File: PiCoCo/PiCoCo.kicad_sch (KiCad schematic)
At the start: 54 parts, among them P1 COCO-CART, Q2 2N7002, Q3 2N7002, Q4 2N7002, U1 Pico 2 / RP2350B-Plus-W, U10 SN74LVC245A, U11 SN74LVC245A, U12 SN74LVC245A, U13 SN74LVC245A, U14 AMS1117-3.3, U15 SN74LVC00A

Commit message: bom: U15 SN74LVC00ADR = LCSC C485072 (schematic, PCB fields, BOM.md, fab package)
Co-Authored-By: Claude Fable 5.1 <noreply@anthropic.com>
Claude-Session: https://claude.ai/code/session_013jbrP69zFzwzxjawTKy2c7
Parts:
- U15: LCSC (none) -> C485072; MPN SN74LVC00AD -> SN74LVC00ADR

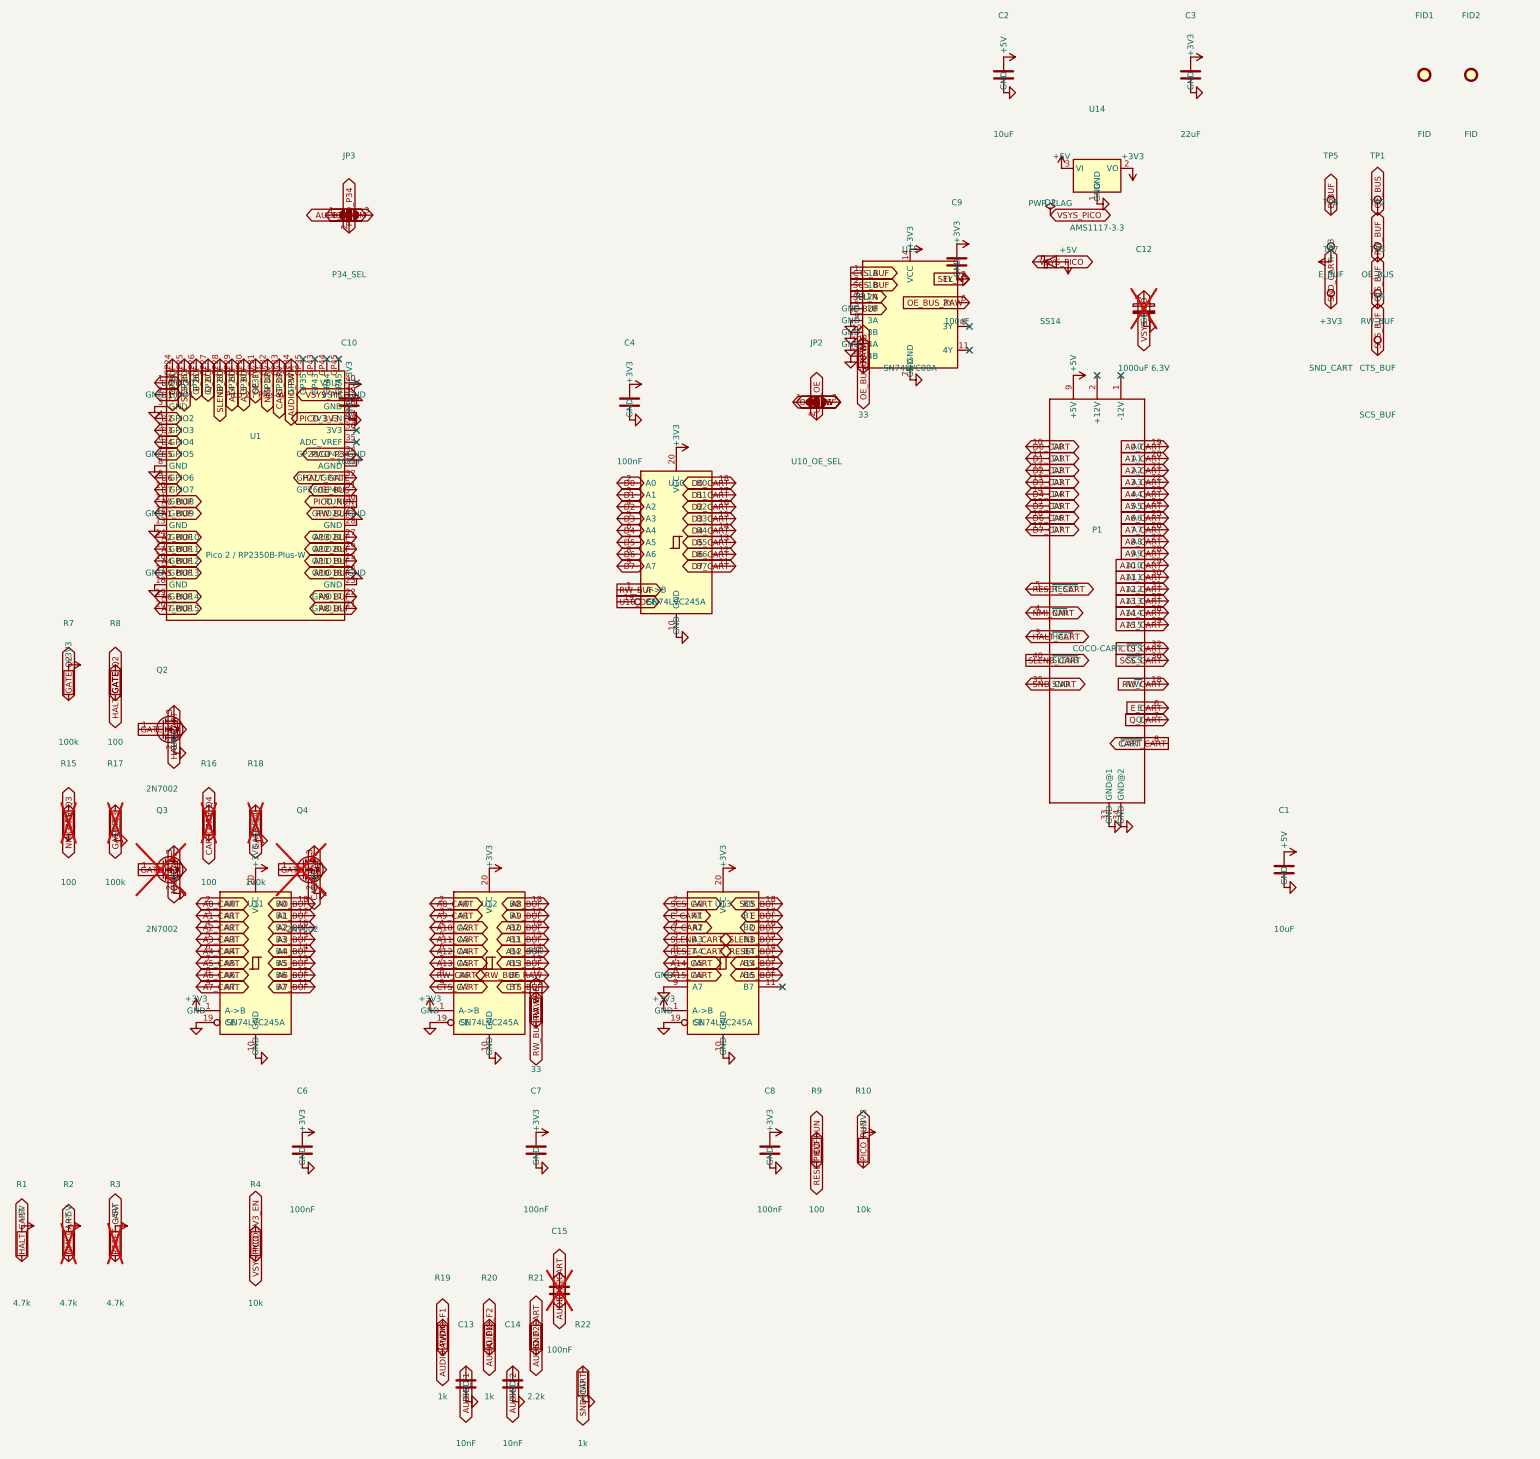
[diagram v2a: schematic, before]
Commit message: v2.3.1: body grown 12 mm, JP3 audio default, pre-order fixes (schematic, outline, docs)
Measured CoCo 3 opening 114.3 x 30.2 mm, connector face 43 mm inside the
case: the 98 mm body fits, but the module USB-C sat on the case surface.
Body is now 98 x 67.16 mm (+10.16 mm tongue); module, TPs, JP3, HDMI
reserve move up 12 mm.

Schematic (gen_schematic.py): R7 10k (RP2350 reset pull-down beat 100k),
R10 DNP (held RUN low when USB-only), R3 populated, R23 10k pull-up on
SLENB_CART (pin 40 is cart->CoCo), R25 10k pull-up on U10_OE, C15 1uF DNP
in series with R24 0R bypass (true AC-coupling option), JP4 Q->/CART
solder jumper (autostart tie), TP8 GND, FID3, JP3 pin 1 = AUDIO_PWM
(audio default), 100k LCSC C149504 (C17407 discontinued). Rev 2.3.1.

Docs, BOM, ordering checklist, breakout README (the tab-width note was
wrong) and spec §11 updated.

Co-Authored-By: Claude Fable 5.1 <noreply@anthropic.com>
Claude-Session: https://claude.ai/code/session_013jbrP69zFzwzxjawTKy2c7
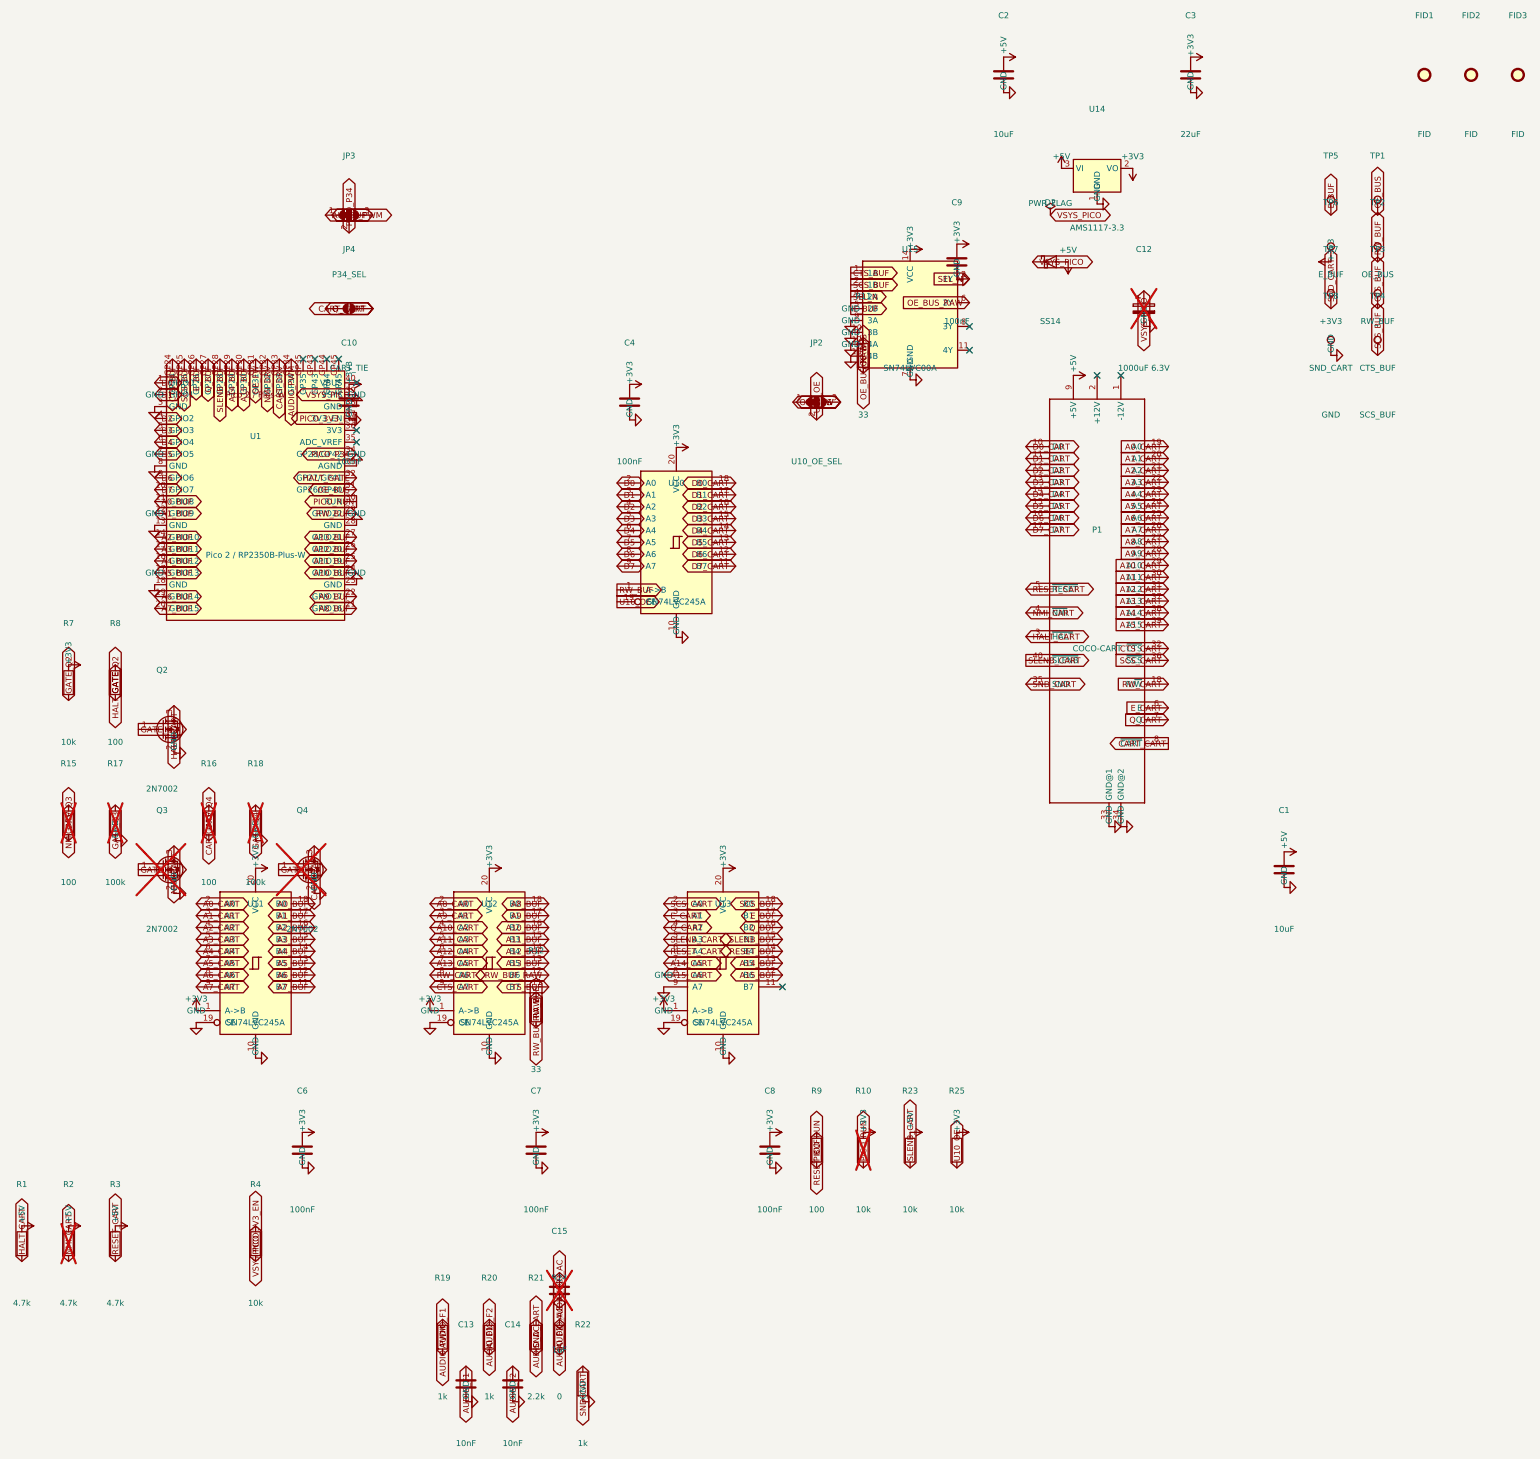
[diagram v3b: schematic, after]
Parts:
- added FID3: FID, Fiducial:Fiducial_1mm_Mask2mm, symbol Mechanical:Fiducial
- added JP4: CART_TIE, Jumper:SolderJumper-2_P1.3mm_Open_RoundedPad1.0x1.5mm, symbol Jumper:SolderJumper_2_Open
- added R23, R25: 10k, Resistor_SMD:R_0805_2012Metric, symbol Device:R
- added R24: 0, Resistor_SMD:R_0805_2012Metric, symbol Device:R
- added TP8: GND, TestPoint:TestPoint_Pad_1.0x1.0mm, symbol Connector:TestPoint
- C15: value 100nF -> 1uF; LCSC C49678 -> C28323; MPN 0805 100nF -> 0805 1uF
- R10: now not fitted
- R17, R18: LCSC C17407 -> C149504
- R3: now fitted
- R7: value 100k -> 10k; LCSC C17407 -> C17414; MPN 0805 100k 1% -> 0805 10k 1%
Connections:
- net +3V3: now also R25.1
- net +5V: now also R23.1
- net AUDIO_F2: now also R24.1; no longer R21.1
- net AUDIO_PWM: now also JP3.1 (A); no longer JP3.3 (B)
- net CART_CART: now also JP4.2 (B)
- net E_BUF: now also JP3.3 (B); no longer JP3.1 (A)
- net GND: now also TP8.1
- net Q_CART: now also JP4.1 (A)
- net SLENB_CART: now also R23.2
- net SND_CART: no longer C15.2
- net U10_OE: now also R25.2
- new net AUDIO_AC: C15.2, R21.1, R24.2

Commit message: v2.3.1: quality-review hardware changes (schematic, rules, tools, docs)
- JP5: header pin 34 -> /CART drive (1-2) or /NMI drive (2-3), open; Q4/R16/R18
  populated so a Pico 2 can pulse /CART under firmware control (JP3 xor JP5).
- J1 EXP (DNP 1x5): Plus-W pads GP35/43/44/45 + GND brought out before the
  module is soldered over them.
- C16 10 uF local bulk at the buffer row; Power netclass 0.5 mm for +5V/+3V3/
  VSYS_PICO.
- Sound stage 470/470/1k/1k (1.1 V pk-pk, -3 dB 18 kHz for the loaded network;
  the old 1k/1k/2.2k gave 0.63 V and 9 kHz).
- Antenna keepout widened to x 151.3..158.0, y 32.7..55.7.
- tools/gnd_stitch.py (per-pad GND vias + 8 mm stitching grid); grid_route and
  finish_route get time budgets.
- Docs: JP5/J1/C16, corrected U13 input list, ROM window -, macro
  name, stale timing claim, HDMI-corner note, README CoCo notes, BOM/checklist.

Co-Authored-By: Claude Fable 5.1 <noreply@anthropic.com>
Claude-Session: https://claude.ai/code/session_013jbrP69zFzwzxjawTKy2c7
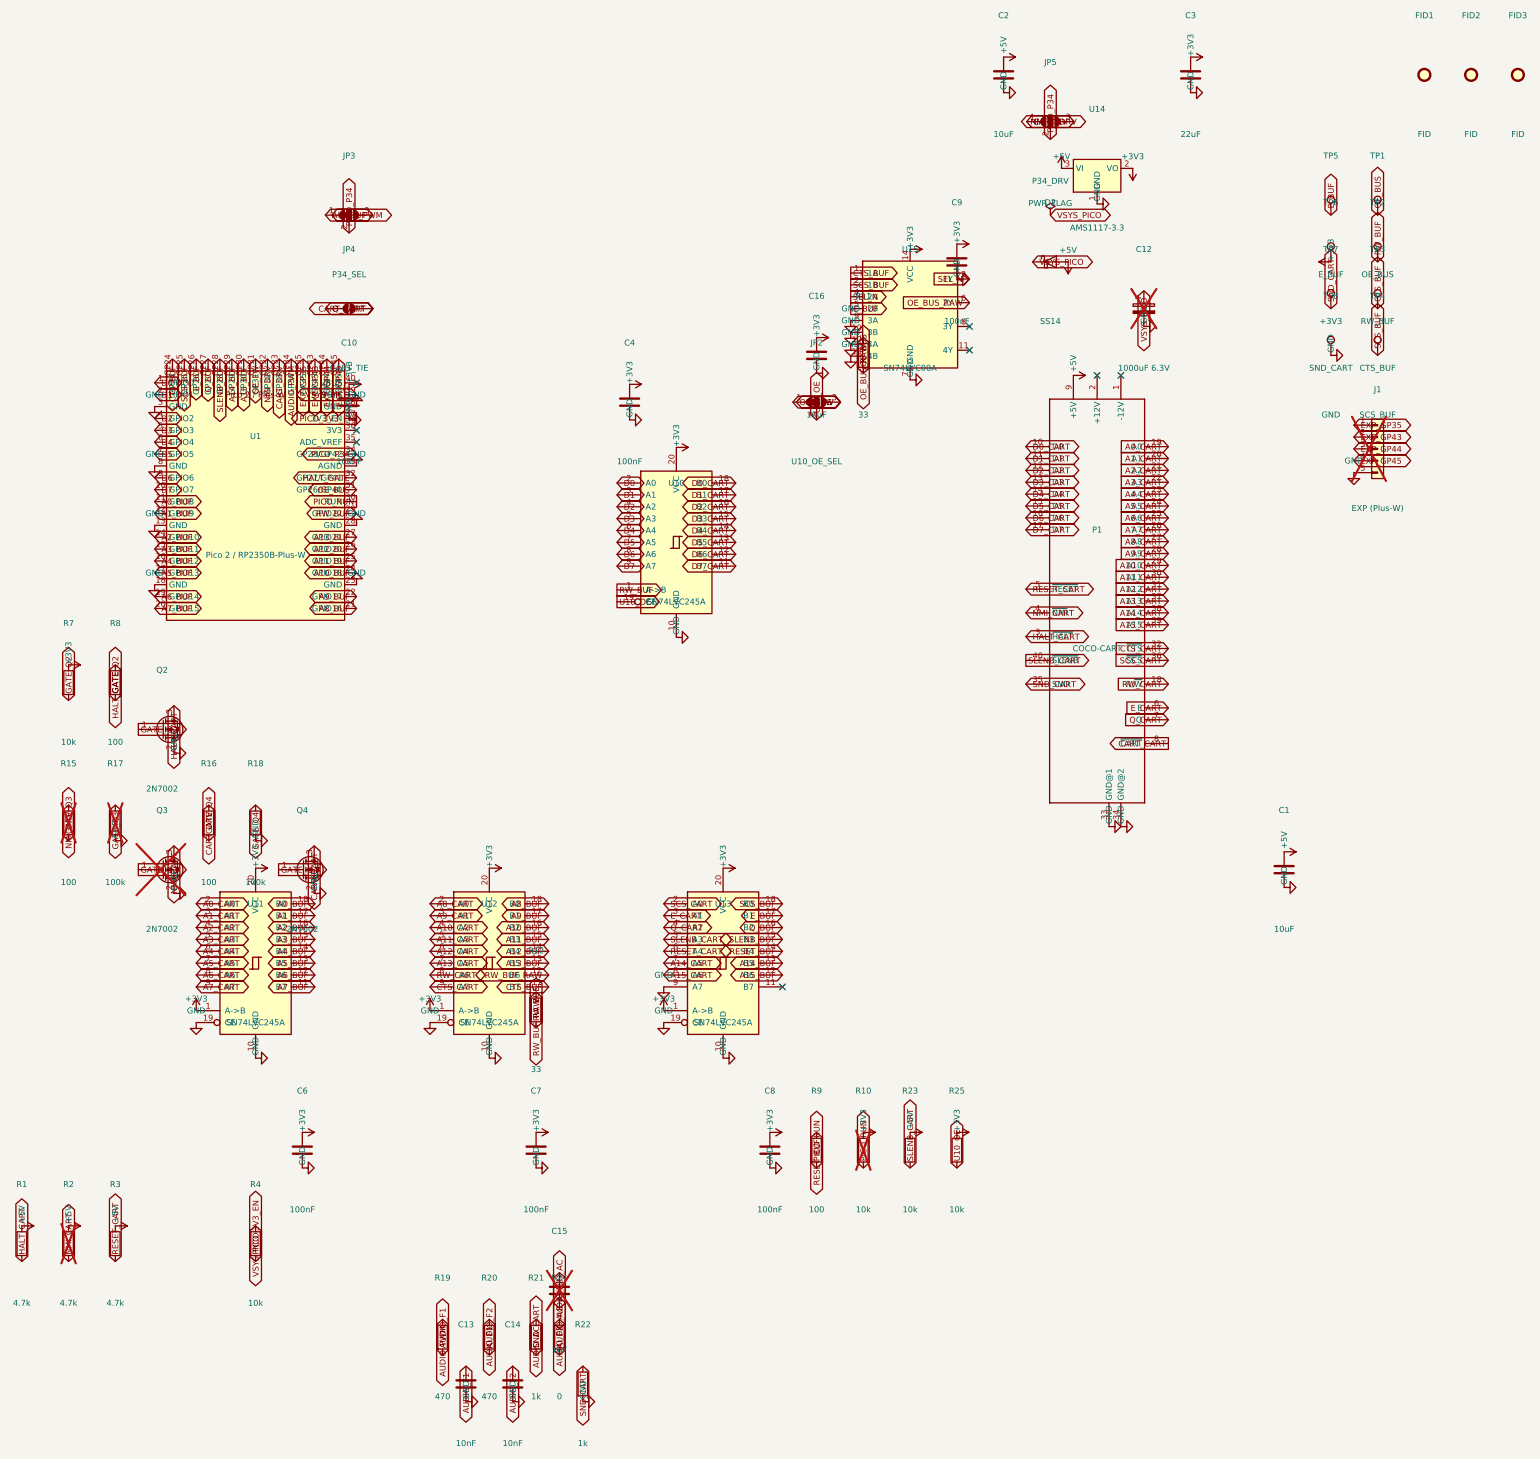
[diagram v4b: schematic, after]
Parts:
- added C16: 10uF, Capacitor_SMD:C_0805_2012Metric, symbol Device:C
- added J1: EXP (Plus-W), Connector_PinHeader_2.54mm:PinHeader_1x05_P2.54mm_Vertical, symbol Connector_Generic:Conn_01x05
- added JP5: P34_DRV, Jumper:SolderJumper-3_P1.3mm_Open_RoundedPad1.0x1.5mm, symbol Jumper:SolderJumper_3_Open
- Q4, R16, R18: now fitted
- R19, R20: value 1k -> 470; LCSC C17513 -> C17710; MPN 0805 1k 1% -> 0805 470 1%
- R21: value 2.2k -> 1k; LCSC C17520 -> C17513; MPN 0805 2.2k 1% -> 0805 1k 1%
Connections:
- net +3V3: now also C16.1
- net CART_DRV: now also JP5.1 (A)
- net GND: now also C16.2, J1.5 (Pin_5)
- net NMI_DRV: now also JP5.3 (B)
- net PICO_P34: now also JP5.2 (C)
- net EXP_GP35: now reaches U1.GP35
- net EXP_GP35: now also J1.1 (Pin_1)
- net EXP_GP43: now reaches U1.GP43
- net EXP_GP43: now also J1.2 (Pin_2)
- net EXP_GP44: now reaches U1.GP44
- net EXP_GP44: now also J1.3 (Pin_3)
- net EXP_GP45: now reaches U1.GP45
- net EXP_GP45: now also J1.4 (Pin_4)
- no-connect marks 12 -> 8
